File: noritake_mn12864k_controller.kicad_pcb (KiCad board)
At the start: 4 copper layers, 85 x 45.5 mm, 148 parts, among them J1 Conn_01x11, J2 USB_C_Receptacle_USB2.0, J3 TagConnect_TC2030_SWD, J4 Conn_01x18, Q1 AO3400A, Q10 2N7002, Q11 LBSS84LT1G, Q12 2N7002, Q13 TO-252, Q14 CJT04N15, Q15 2N7002, Q16 LBSS84LT1G, Q17 2N7002, Q18 S9015, Q2 AO3400A, Q3 S9015, Q4 AO3401A, Q5 AO3401A, Q6 S9015, Q7 2N7002, Q8 LBSS84LT1G, Q9 2N7002, T1 Wuerth 760390013, T2 Wuerth 760390013, T3 Wuerth 760390013, U1 SN74AVC8T245PW, U10 SRV05-4, U11 SRV05-4, U12 SRV05-4, U2 74HC14, U3 CD4051B, U4 MN12864K, U5 STM32F730R8T6, U6 NE555D, U7 74HC08, U8 SRV05-4, U9 XC6206PxxxMR

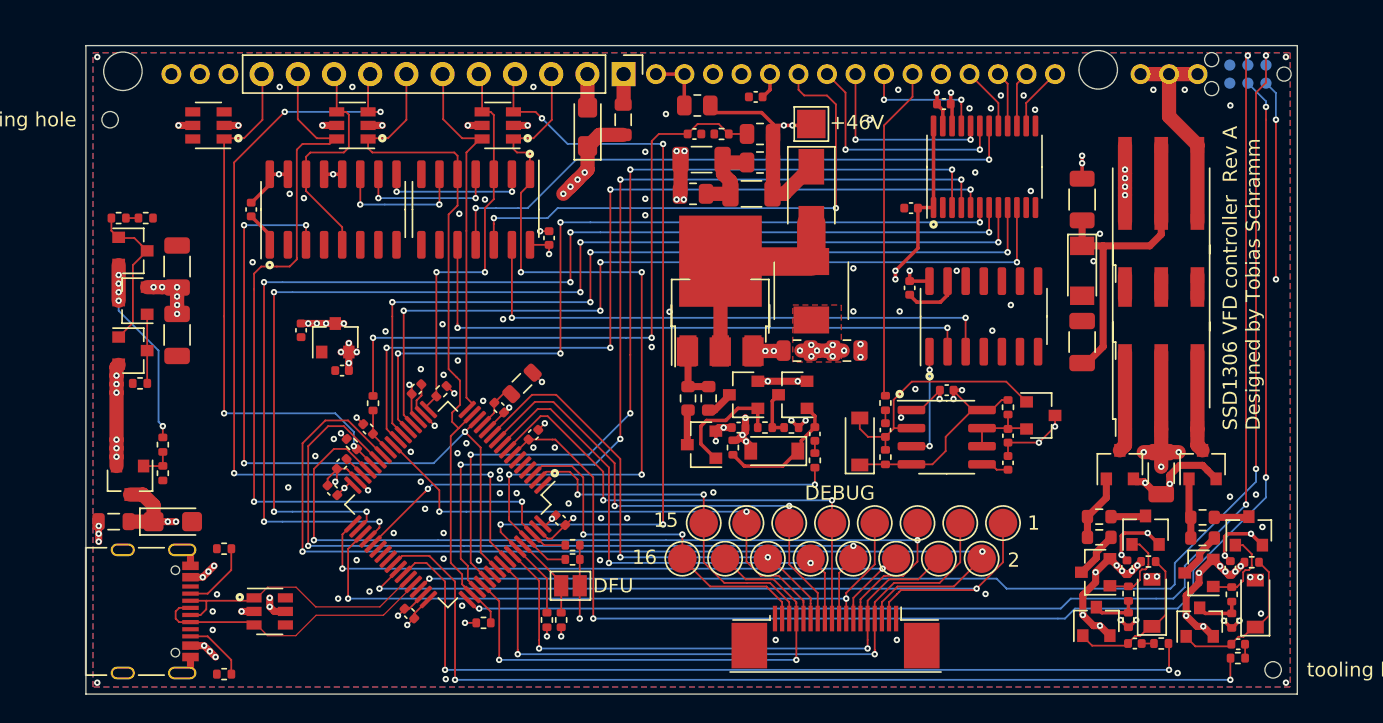
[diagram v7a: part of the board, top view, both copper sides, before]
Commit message: Add pin labels
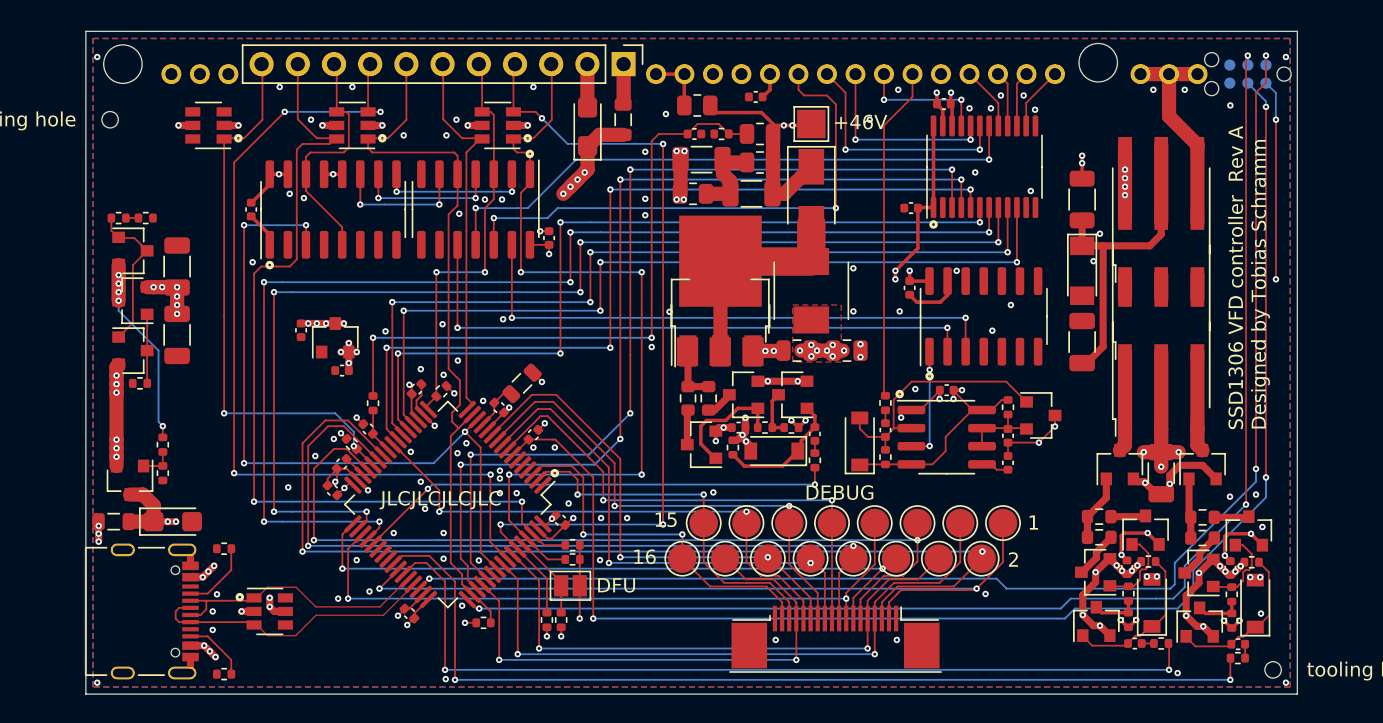
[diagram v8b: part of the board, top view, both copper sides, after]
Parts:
- moved J1 0.70 mm to (137.7, 97.8)
- moved H3 0.50 mm to (171.0, 97.7)
- moved H4 0.50 mm to (102.6, 97.8)
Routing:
- net /~RST: track 27.7 -> 28.8 mm
- net /~DC: track 25.7 -> 26.7 mm
- net /4WIRE: track 59.6 -> 60.5 mm
- net /~SHDWN: track 38.2 -> 39.2 mm
- net /~CS: track 50.2 -> 51.1 mm
- net /SCK: track 16.4 -> 17.2 mm
- net /IFSEL: track 60.7 -> 61.5 mm
- net /MOSI: track 61.6 -> 62.3 mm
- net GND: vias 137 -> 142
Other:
- board size 85 x 45.5 mm -> 85 x 46.5 mm
- board text added: "+5V"
- board text added: "DI"
- board text added: "GND"
- board text added: "JLCJLCJLCJLC"
- board text added: "SCK"
- board text added: "SCL"
- board text added: "SDA"
- board text added: "SEL"
- board text added: "~CS"
- board text added: "~DC"
- board text added: "~RST"
- board text added: "~SHD"
